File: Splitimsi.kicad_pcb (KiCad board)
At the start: 2 copper layers, 118.2 x 100.1 mm, 34 parts, among them SW1 MX_RGB, SW10 MX_RGB, SW11 MX_RGB, SW12 MX_RGB, SW13 MX_RGB, SW14 MX_RGB, SW15 MX_RGB, SW16 RotaryEncoder_Switch, SW17 MX_RGB, SW18 MX_RGB, SW19 MX_RGB, SW2 MX_RGB, SW20 MX_RGB, SW21 MX_RGB, SW22 MX_RGB, SW23 MX_RGB, SW24 MX_RGB, SW25 MX_RGB, SW26 MX_RGB, SW27 MX_RGB, SW28 MX_RGB, SW3 MX_RGB, SW4 MX_RGB, SW5 MX_RGB, SW6 MX_RGB, SW7 MX_RGB, SW8 MX_RGB, SW9 MX_RGB, U1 ProMicro, U2 TRRS

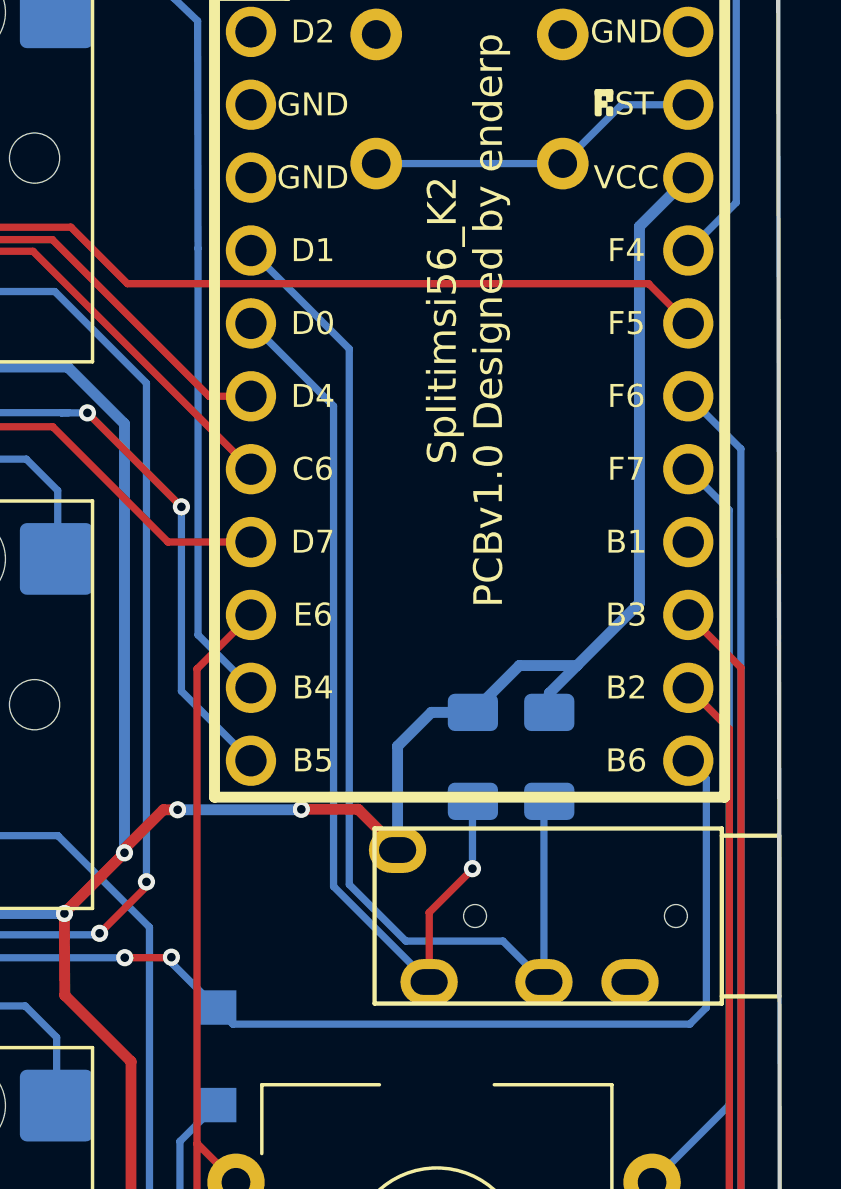
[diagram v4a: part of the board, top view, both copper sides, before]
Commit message: trrs resistors places changed
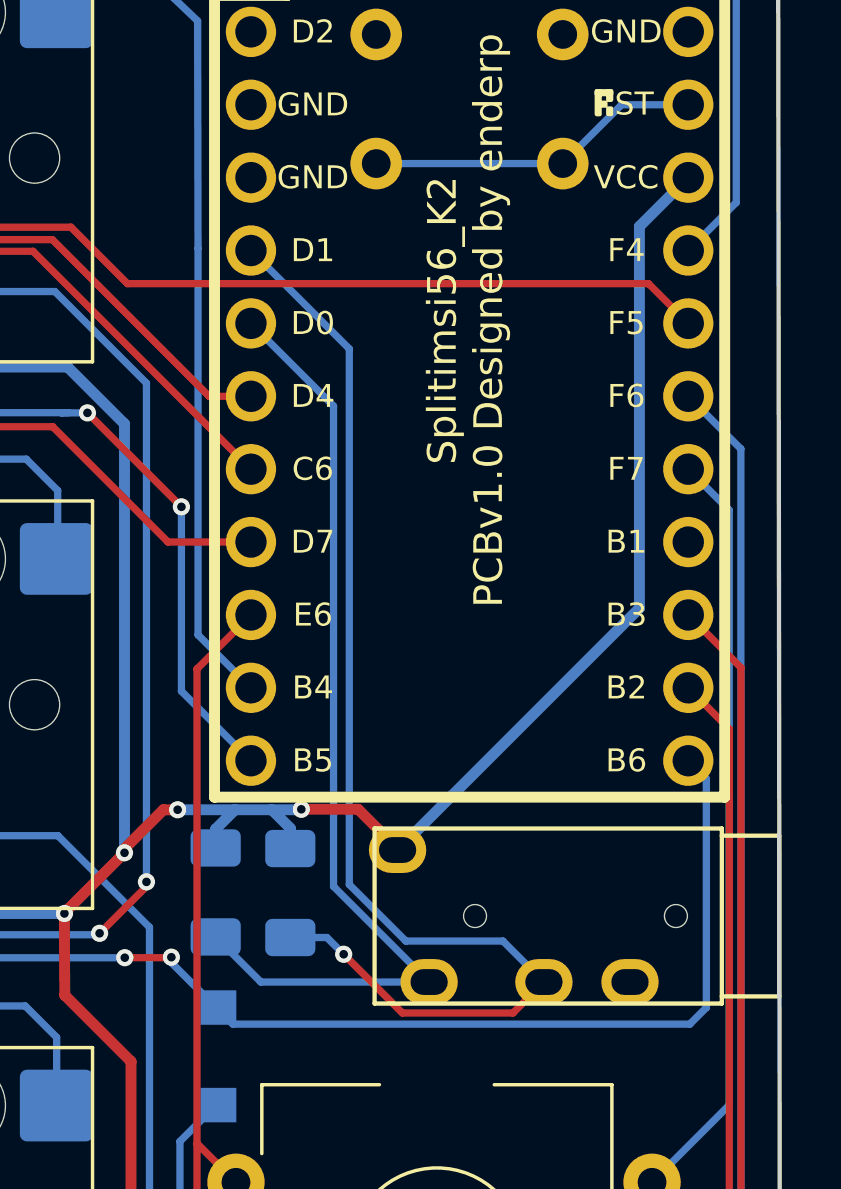
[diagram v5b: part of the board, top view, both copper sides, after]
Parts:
- moved R1 10.2 mm to (121.3, 54.2)
- moved R2 10.1 mm to (118.7, 54.2)
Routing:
- net /SDA: track 38.1 -> 42.1 mm, vias 0 -> 1
- net /SCL: track 32.5 -> 33.6 mm, vias 1 -> 0
- net +5V: track 601.9 -> 601.1 mm

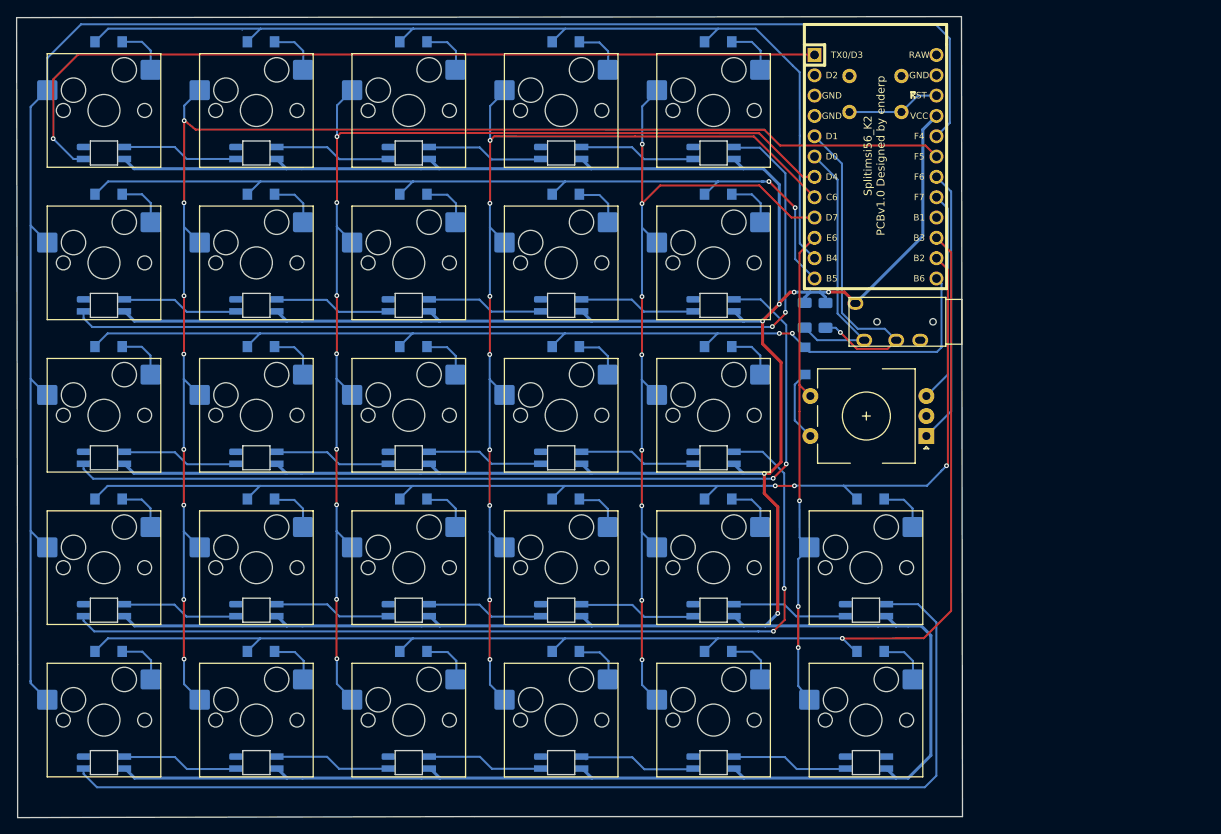
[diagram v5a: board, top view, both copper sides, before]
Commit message: TRRS update
- TRRS resistor tracks reorganized
- Jack position reorganized
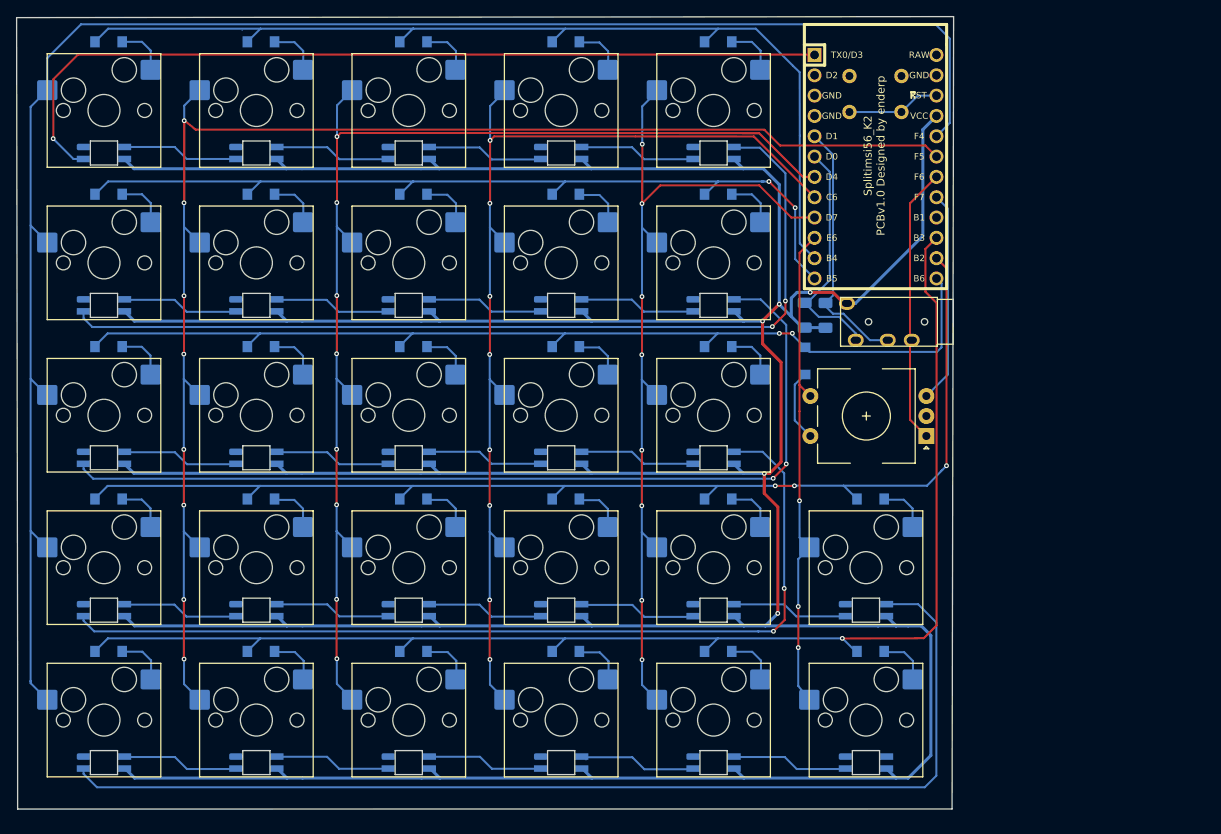
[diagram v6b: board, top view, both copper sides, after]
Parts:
- moved U2 1.06 mm to (135.3, 55.0)
- turned R1 to 90 degrees
- turned R2 to 90 degrees
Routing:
- net /SDA: track 42.1 -> 31.6 mm, vias 1 -> 0
- net +5V: track 601.1 -> 605.4 mm, vias 6 -> 5
- net /SCL: track 33.6 -> 29.4 mm
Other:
- board size 118.2 x 100.1 mm -> 117.1 x 99.1 mm

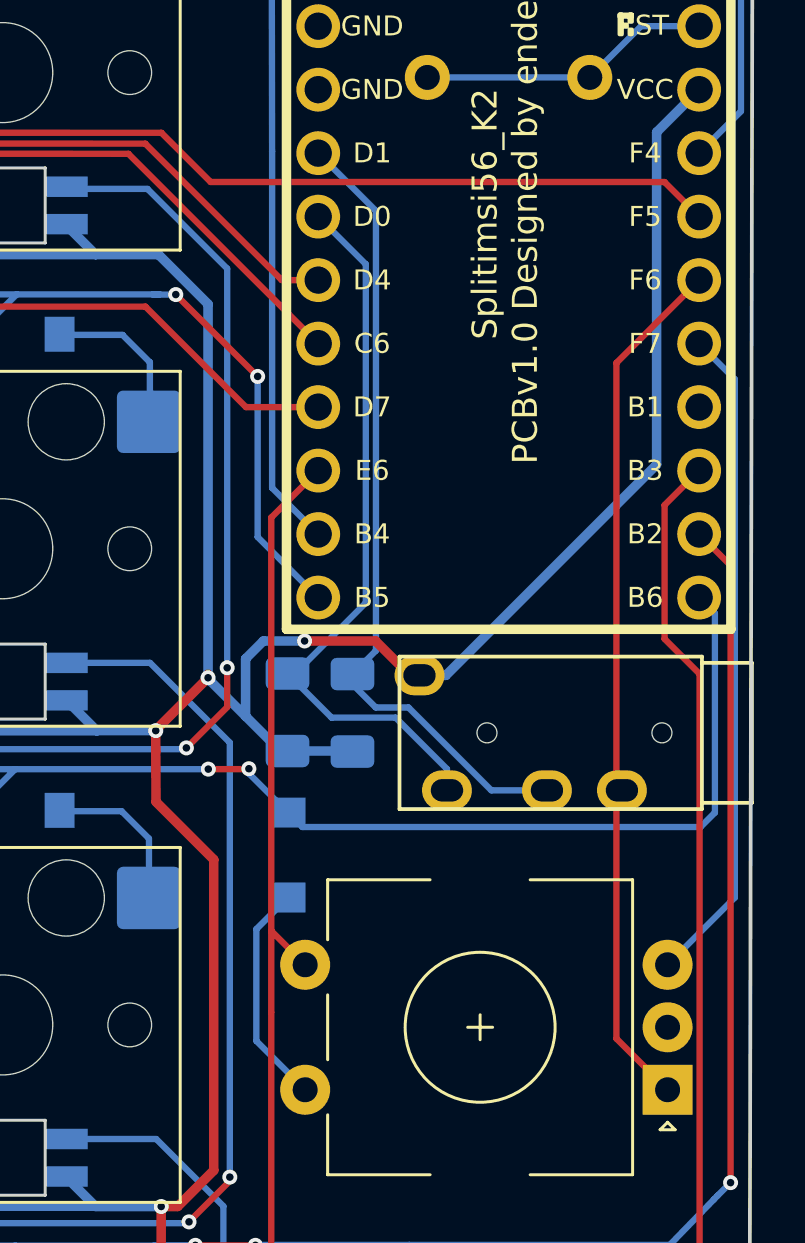
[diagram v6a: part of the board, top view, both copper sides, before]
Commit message: Track bugs fixed
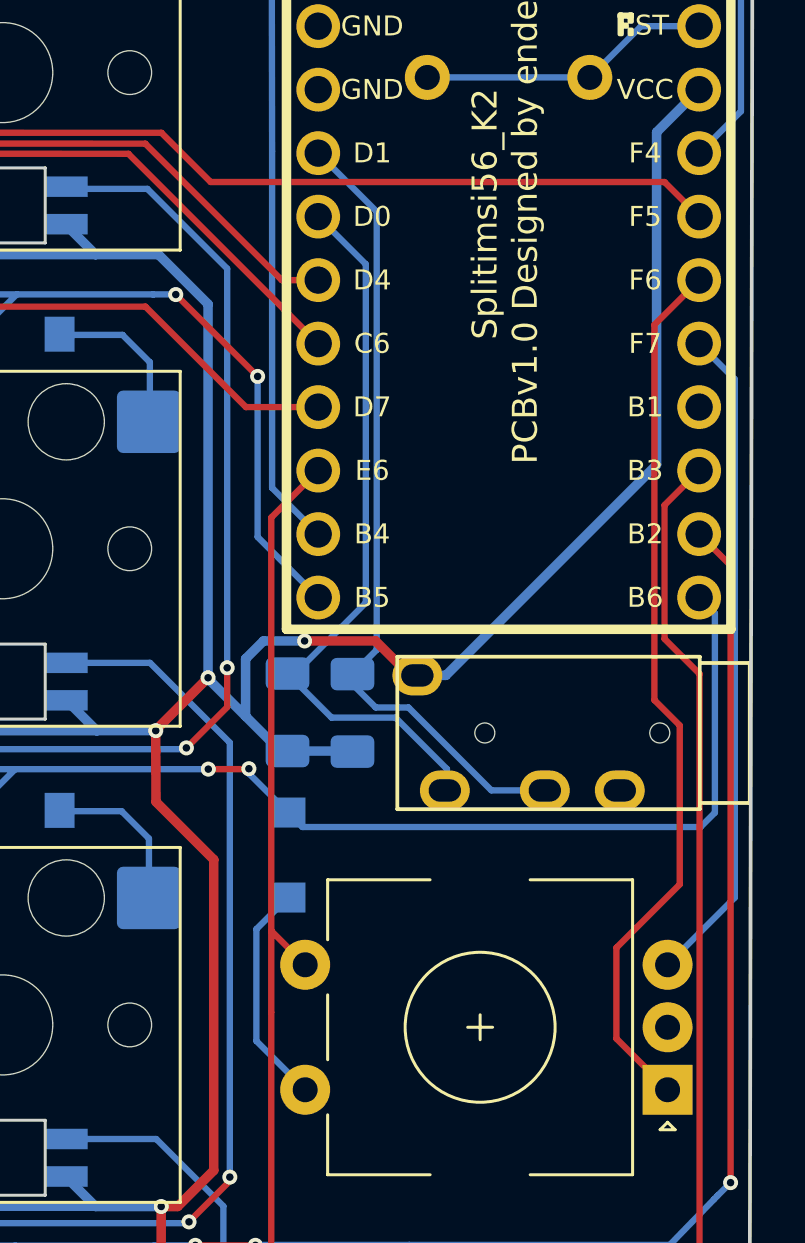
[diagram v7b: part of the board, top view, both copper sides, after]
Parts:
- moved U2 0.09 mm to (135.2, 55.0)
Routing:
- net /RotPinA: track 34.6 -> 35.4 mm
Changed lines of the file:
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@@
   )
   (footprint "Keebio-Parts:TRRS-PJ-320A" (layer "F.Cu")
-    (at 135.2875 54.989572 -90)
+    (at 135.201465 54.994246 -90)
     (property "Sheetfile" "Splitimsi.kicad_sch")
     (property "Sheetname" "")
@@
   )
   (footprint "Resistor_SMD:R_1206_3216Metric_Pad1.30x1.75mm_HandSolder" (layer "B.Cu")
-    (at 121.306216 54.188573 90)
+    (at 121.30585 54.190251 90)
     (descr "Resistor SMD 1206 (3216 Metric), square (rectangular) end terminal, IPC_7351 nominal with elongated pad for handsoldering. (Body size source: IPC-SM-782 page 72, https://www.pcb-3d.com/wordpress/wp-content/uploads/ipc-sm-782a_amendment_1_and_2.pdf), generated with kicad-footprint-generator")
     (tags "resistor handsolder")
@@
     (property "Sheetname" "")
     (attr smd)
-    (fp_text reference "R2" (at 0 1.82 90) (layer "B.SilkS")
+    (fp_text reference "R2" (at -3.363753 2.928928 90) (layer "B.SilkS")
       (effects (font (size 1 1) (thickness 0.15)) (justify mirror))
     )
@@
   (segment (start 115.338651 78.132137) (end 115.338651 91.440264) (width 0.381) (layer "F.Cu") (net 3))
   (segment (start 113.435823 55.725971) (end 113.447545 57.751205) (width 0.381) (layer "F.Cu") (net 3))
-  (segment (start 115.52872 52.78557) (end 115.52872 52.64281) (width 0.381) (layer "F.Cu") (net 3))
   (segment (start 115.756995 60.060655) (end 115.756995 72.497178) (width 0.381) (layer "F.Cu") (net 3))
   (segment (start 123.605826 52.689572) (end 122.229796 51.313542) (width 0.381) (layer "F.Cu") (net 3))
@@
   (segment (start 129.0875 57.289572) (end 126.861677 57.289572) (width 0.254) (layer "B.Cu") (net 61))
   (segment (start 126.861677 57.289572) (end 123.547105 53.975) (width 0.254) (layer "B.Cu") (net 61))
-  (segment (start 122.245335 51.699454) (end 121.306216 52.638573) (width 0.254) (layer "B.Cu") (net 61))
+  (segment (start 122.274895 34.135737) (end 122.274895 51.669894) (width 0.254) (layer "B.Cu") (net 61))
+  (segment (start 122.274895 51.669894) (end 121.306216 52.638573) (width 0.254) (layer "B.Cu") (net 61))
+  (segment (start 119.936143 31.796985) (end 122.274895 34.135737) (width 0.254) (layer "B.Cu") (net 61))
   (segment (start 123.547105 53.975) (end 122.2375 53.975) (width 0.254) (layer "B.Cu") (net 61))
-  (segment (start 122.245335 34.106177) (end 122.245335 51.699454) (width 0.254) (layer "B.Cu") (net 61))
   (segment (start 121.357215 52.689572) (end 121.306216 52.638573) (width 0.381) (layer "B.Cu") (net 61))
-  (segment (start 119.936143 31.796985) (end 122.245335 34.106177) (width 0.254) (layer "B.Cu") (net 61))
   (segment (start 97.546102 31.813394) (end 112.342757 31.823599) (width 0.254) (layer "F.Cu") (net 63))
   (segment (start 79.892194 31.801219) (end 97.546102 31.813394) (width 0.254) (layer "F.Cu") (net 63))
@@
   (segment (start 98.342968 81.291795) (end 100.328819 83.277646) (width 0.254) (layer "B.Cu") (net 64))
   (segment (start 98.369171 43.217998) (end 98.369171 51.840431) (width 0.254) (layer "B.Cu") (net 64))
-  (segment (start 133.913882 69.268847) (end 131.866597 67.221562) (width 0.254) (layer "F.Cu") (net 66))
-  (segment (start 131.866597 67.221562) (end 131.866597 40.186531) (width 0.254) (layer "F.Cu") (net 66))
-  (segment (start 131.866597 40.186531) (end 135.176143 36.876985) (width 0.254) (layer "F.Cu") (net 66))
+  (segment (start 133.3865 38.666628) (end 133.3865 53.681113) (width 0.254) (layer "F.Cu") (net 66))
+  (segment (start 131.866597 67.221562) (end 133.913882 69.268847) (width 0.254) (layer "F.Cu") (net 66))
+  (segment (start 133.3865 53.681113) (end 134.398811 54.693424) (width 0.254) (layer "F.Cu") (net 66))
+  (segment (start 134.398811 54.693424) (end 134.398811 61.052717) (width 0.254) (layer "F.Cu") (net 66))
+  (segment (start 134.398811 61.052717) (end 131.866597 63.584931) (width 0.254) (layer "F.Cu") (net 66))
+  (segment (start 131.866597 63.584931) (end 131.866597 67.221562) (width 0.254) (layer "F.Cu") (net 66))
+  (segment (start 135.176143 36.876985) (end 133.3865 38.666628) (width 0.254) (layer "F.Cu") (net 66))
   (segment (start 135.176143 39.416985) (end 136.603356 40.844198) (width 0.254) (layer "B.Cu") (net 67))
   (segment (start 136.603356 61.579373) (end 133.913882 64.268847) (width 0.254) (layer "B.Cu") (net 67))
@@
   (via (at 117.512368 40.729531) (size 0.6) (drill 0.3) (layers "F.Cu" "B.Cu") (net 68))
   (segment (start 119.936143 49.576985) (end 117.512368 47.15321) (width 0.254) (layer "B.Cu") (net 68))
+  (segment (start 114.230866 37.448029) (end 114.237354 37.454517) (width 0.254) (layer "B.Cu") (net 68))
   (segment (start 107.872659 37.448029) (end 113.331713 37.448029) (width 0.254) (layer "B.Cu") (net 68))
   (segment (start 31.628844 37.448029) (end 50.678844 37.448029) (width 0.254) (layer "B.Cu") (net 68))
-  (segment (start 113.331713 37.448029) (end 113.592215 37.448029) (width 0.254) (layer "B.Cu") (net 68))
   (segment (start 50.678844 37.448029) (end 69.799937 37.448029) (width 0.254) (layer "B.Cu") (net 68))
   (segment (start 29.986637 39.090236) (end 31.628844 37.448029) (width 0.254) (layer "B.Cu") (net 68))
   (segment (start 106.230452 39.090236) (end 107.872659 37.448029) (width 0.254) (layer "B.Cu") (net 68))
-  (segment (start 114.237354 37.454517) (end 113.338201 37.454517) (width 0.254) (layer "B.Cu") (net 68))
+  (segment (start 113.331713 37.448029) (end 114.230866 37.448029) (width 0.254) (layer "B.Cu") (net 68))
   (segment (start 88.768329 37.448029) (end 107.872659 37.448029) (width 0.254) (layer "B.Cu") (net 68))
   (segment (start 117.512368 47.15321) (end 117.512368 40.729531) (width 0.254) (layer "B.Cu") (net 68))
